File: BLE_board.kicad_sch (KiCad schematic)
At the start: 0 parts

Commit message: First basic design
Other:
- added sheet USB and Power (usb_module.kicad_sch)
- sheet MCU Module ports: added RF_CE, RF_IRQ, USB_D+, USB_D-; removed none
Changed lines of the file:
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@@
+	(wire
+		(pts
+			(xy 76.454 44.45) (xy 104.648 44.45)
+		)
+		(stroke
+			(width 0)
+			(type default)
+		)
+	)
 	(wire
 		(pts
@@
 	(wire
 		(pts
+			(xy 55.88 51.054) (xy 55.88 58.674)
+		)
+		(stroke
+			(width 0)
+			(type default)
+		)
+	)
+	(wire
+		(pts
 			(xy 76.454 39.37) (xy 104.648 39.37)
 		)
@@
 			(width 0)
 			(type default)
+		)
+	)
+	(wire
+		(pts
+			(xy 58.42 51.054) (xy 58.42 58.674)
+		)
+		(stroke
+			(width 0)
+			(type default)
+		)
+	)
+	(wire
+		(pts
+			(xy 76.454 41.91) (xy 104.648 41.91)
+		)
+		(stroke
+			(width 0)
+			(type default)
+		)
+	)
+	(sheet
+		(at 24.384 58.674)
+		(size 51.308 23.876)
+		(fields_autoplaced yes)
+		(stroke
+			(width 0.1524)
+			(type solid)
+		)
+		(fill
+			(color 0 0 0 0.0000)
+		)
+		(property "Sheetname" "USB and Power"
+			(at 24.384 57.9624 0)
+			(effects
+				(font
+					(size 1.27 1.27)
+				)
+				(justify left bottom)
+			)
+		)
+		(property "Sheetfile" "usb_module.kicad_sch"
+			(at 24.384 83.1346 0)
+			(effects
+				(font
+					(size 1.27 1.27)
+				)
+				(justify left top)
+			)
+		)
+		(pin "USB_D+" input
+			(at 55.88 58.674 90)
+			(effects
+				(font
+					(size 1.27 1.27)
+				)
+				(justify right)
+			)
+		)
+		(pin "USB_D-" input
+			(at 58.42 58.674 90)
+			(effects
+				(font
+					(size 1.27 1.27)
+				)
+				(justify right)
+			)
+		)
+		(instances
+			(project "BLE_board"
+				(path "/75856061-4be0-4eb9-8c9e-0f2487affa58"
+					(page "4")
+				)
+			)
 		)
 	)
@@
 			)
 		)
+		(pin "RF_CE" input
+			(at 76.454 44.45 0)
+			(effects
+				(font
+					(size 1.27 1.27)
+				)
+				(justify right)
+			)
+		)
+		(pin "RF_IRQ" input
+			(at 76.454 41.91 0)
+			(effects
+				(font
+					(size 1.27 1.27)
+				)
+				(justify right)
+			)
+		)
+		(pin "USB_D+" input
+			(at 55.88 51.054 270)
+			(effects
+				(font
+					(size 1.27 1.27)
+				)
+				(justify left)
+			)
+		)
+		(pin "USB_D-" input
+			(at 58.42 51.054 270)
+			(effects
+				(font
+					(size 1.27 1.27)
+				)
+				(justify left)
+			)
+		)

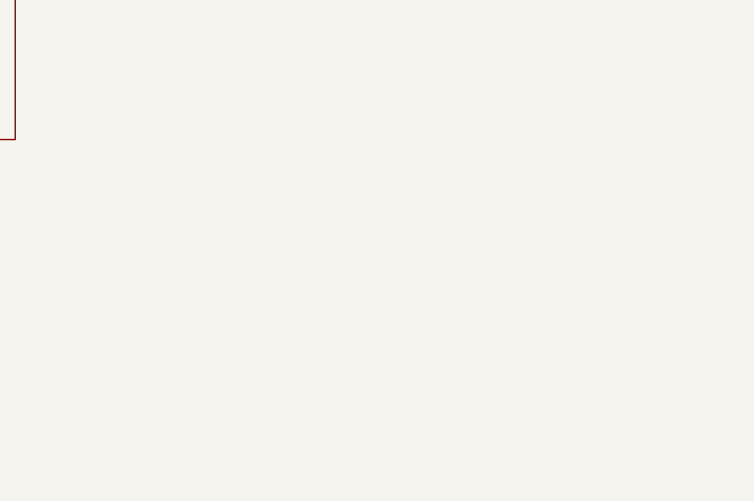
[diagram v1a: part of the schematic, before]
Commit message: Larger dimensions. Include mounting holes. Better antenna feed alignment
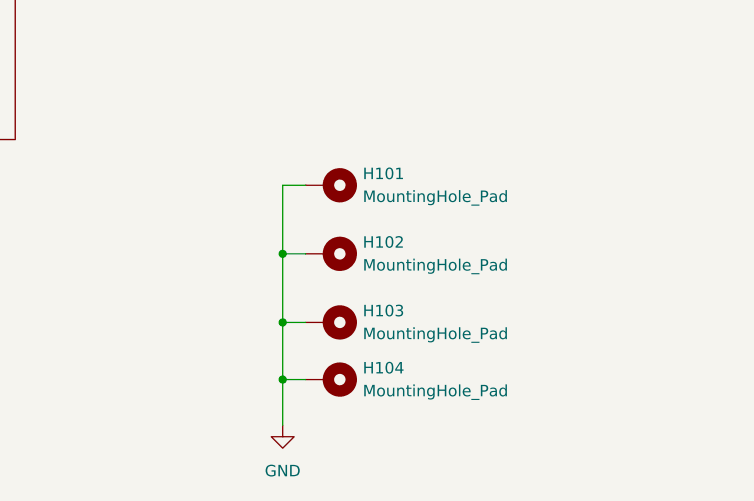
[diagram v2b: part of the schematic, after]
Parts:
- added H101, H102, H103, H104: MountingHole_Pad, MountingHole:MountingHole_2.2mm_M2_Pad, symbol Mechanical:MountingHole_Pad
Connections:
- new net GND: H101.1, H102.1, H103.1, H104.1
